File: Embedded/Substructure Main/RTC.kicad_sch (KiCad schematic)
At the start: 6 parts, among them J3 Coin Cell, U5 MCP7940N-xMNY, Y2 32.768KHz 8pf

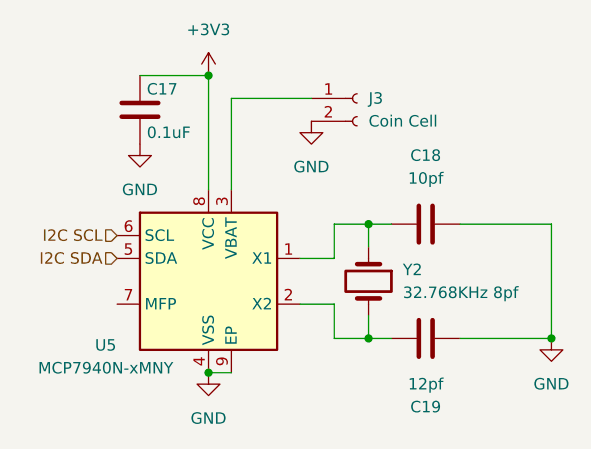
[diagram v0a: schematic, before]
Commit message: Added LDOs and Modified Component Names
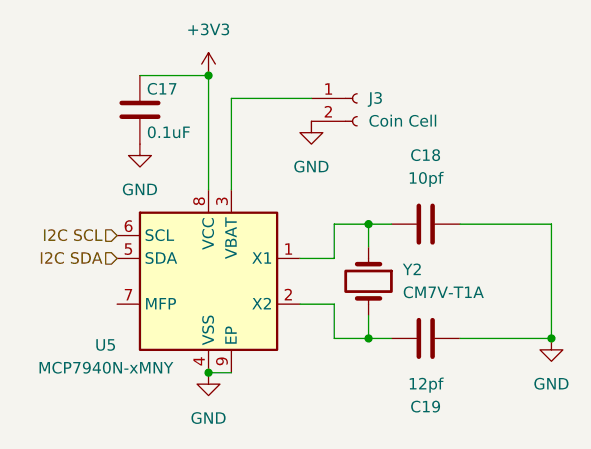
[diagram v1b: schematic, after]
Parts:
- Y2: value 32.768KHz 8pf -> CM7V-T1A
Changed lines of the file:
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@@
 			)
 		)
-		(property "Value" "32.768KHz 8pf"
+		(property "Value" "CM7V-T1A"
 			(at 105.41 72.3899 90)
 			(effects

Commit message: Added Boot Switch Selection & Sensor Array
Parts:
- J3: footprint (none) -> Connector_JST:JST_ZH_B2B-ZR_1x02_P1.50mm_Vertical
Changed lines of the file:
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@@
 			)
 		)
-		(property "Footprint" ""
+		(property "Footprint" "Connector_JST:JST_ZH_B2B-ZR_1x02_P1.50mm_Vertical"
 			(at 100.33 50.8 0)
 			(effects

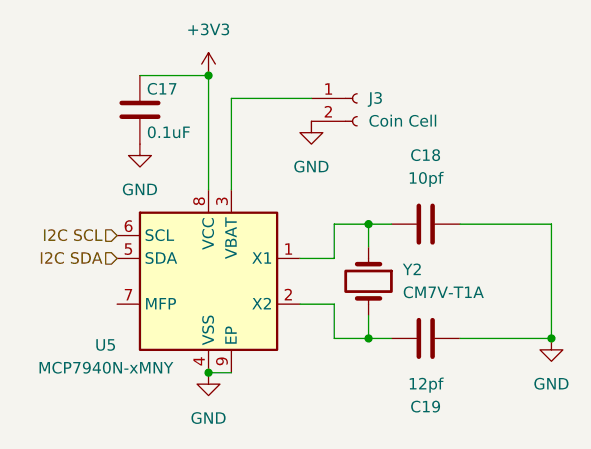
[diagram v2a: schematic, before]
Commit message: Added Sensored V2 Board
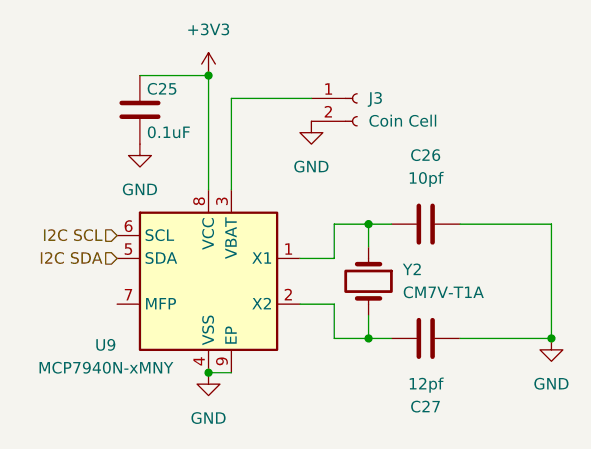
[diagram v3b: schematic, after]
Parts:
- renumbered C17 to C25, C18 to C26, C19 to C27, U5 to U9
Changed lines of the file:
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@@
 		(dnp no)
 		(fields_autoplaced yes)
-		(property "Reference" "#PWR054"
+		(property "Reference" "#PWR072"
 			(at 121.92 83.82 0)
 			(effects
@@
 			(project "Substructure Main"
 				(path "/dda3f9ed-866a-496e-a4f2-d6745d13652e/cf64468b-2af6-4e81-8dd0-6dc57a236030"
-					(reference "#PWR054")
+					(reference "#PWR072")
 					(unit 1)
 				)
@@
 		(on_board yes)
 		(dnp no)
-		(property "Reference" "C17"
+		(property "Reference" "C25"
 			(at 76.962 49.784 0)
 			(effects
@@
 			(project "Substructure Main"
 				(path "/dda3f9ed-866a-496e-a4f2-d6745d13652e/cf64468b-2af6-4e81-8dd0-6dc57a236030"
-					(reference "C17")
+					(reference "C25")
 					(unit 1)
 				)
@@
 		(on_board yes)
 		(dnp no)
-		(property "Reference" "U5"
+		(property "Reference" "U9"
 			(at 72.39 78.232 0)
 			(effects
@@
 			(project "Substructure Main"
 				(path "/dda3f9ed-866a-496e-a4f2-d6745d13652e/cf64468b-2af6-4e81-8dd0-6dc57a236030"
-					(reference "U5")
+					(reference "U9")
 					(unit 1)
 				)
@@
 		(dnp no)
 		(fields_autoplaced yes)
-		(property "Reference" "#PWR035"
+		(property "Reference" "#PWR069"
 			(at 83.82 52.07 0)
 			(effects
@@
 			(project "Substructure Main"
 				(path "/dda3f9ed-866a-496e-a4f2-d6745d13652e/cf64468b-2af6-4e81-8dd0-6dc57a236030"
-					(reference "#PWR035")
+					(reference "#PWR069")
 					(unit 1)
 				)
@@
 		(dnp no)
 		(fields_autoplaced yes)
-		(property "Reference" "#PWR046"
+		(property "Reference" "#PWR071"
 			(at 95.25 59.69 0)
 			(effects
@@
 			(project "Substructure Main"
 				(path "/dda3f9ed-866a-496e-a4f2-d6745d13652e/cf64468b-2af6-4e81-8dd0-6dc57a236030"
-					(reference "#PWR046")
+					(reference "#PWR071")
 					(unit 1)
 				)
@@
 		(on_board yes)
 		(dnp no)
-		(property "Reference" "C19"
+		(property "Reference" "C27"
 			(at 107.95 85.09 90)
 			(effects
@@
 			(project "Substructure Main"
 				(path "/dda3f9ed-866a-496e-a4f2-d6745d13652e/cf64468b-2af6-4e81-8dd0-6dc57a236030"
-					(reference "C19")
+					(reference "C27")
 					(unit 1)
 				)
@@
 		(dnp no)
 		(fields_autoplaced yes)
-		(property "Reference" "#PWR030"
+		(property "Reference" "#PWR068"
 			(at 76.2 62.23 0)
 			(effects
@@
 			(project "Substructure Main"
 				(path "/dda3f9ed-866a-496e-a4f2-d6745d13652e/cf64468b-2af6-4e81-8dd0-6dc57a236030"
-					(reference "#PWR030")
+					(reference "#PWR068")
 					(unit 1)
 				)
@@
 		(dnp no)
 		(fields_autoplaced yes)
-		(property "Reference" "#PWR045"
+		(property "Reference" "#PWR070"
 			(at 83.82 87.63 0)
 			(effects
@@
 			(project "Substructure Main"
 				(path "/dda3f9ed-866a-496e-a4f2-d6745d13652e/cf64468b-2af6-4e81-8dd0-6dc57a236030"
-					(reference "#PWR045")
+					(reference "#PWR070")
 					(unit 1)
 				)
@@
 		(dnp no)
 		(fields_autoplaced yes)
-		(property "Reference" "C18"
+		(property "Reference" "C26"
 			(at 107.95 57.15 90)
 			(effects
@@
 			(project "Substructure Main"
 				(path "/dda3f9ed-866a-496e-a4f2-d6745d13652e/cf64468b-2af6-4e81-8dd0-6dc57a236030"
-					(reference "C18")
-					(unit 1)
-				)
+					(reference "C26")
+					(unit 1)
+				)
